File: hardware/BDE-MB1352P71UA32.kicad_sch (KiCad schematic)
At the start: 11 parts, among them J22 Conn_ARM_JTAG_SWD_10, SW1 SW_Push, U1 USBLC6-2P6, U23 BDE-MB1352P71UA32, U3 USBLC6-2P6

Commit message: updated annotations
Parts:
- renumbered C1 to C401, C10 to C402, C2 to C403, D7 to D401, J22 to J401, R7 to R401, R3 to R402, SW1 to SW401, U1 to U401, U3 to U402, U23 to U403
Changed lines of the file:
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@@
 		(dnp no)
 		(fields_autoplaced yes)
-		(property "Reference" "#PWR075"
+		(property "Reference" "#PWR0409"
 			(at 142.24 143.51 0)
 			(effects
@@
 			(project "Senior_Design"
 				(path "/8f5928e8-0fc1-4443-a20f-3bfeb956761e/dd2813e4-a810-44d7-8b7e-d46ce1c3fa30"
-					(reference "#PWR075")
+					(reference "#PWR0409")
 					(unit 1)
 				)
@@
 		(dnp no)
 		(fields_autoplaced yes)
-		(property "Reference" "#PWR072"
+		(property "Reference" "#PWR0411"
 			(at 152.4 78.74 0)
 			(effects
@@
 			(project "Senior_Design"
 				(path "/8f5928e8-0fc1-4443-a20f-3bfeb956761e/dd2813e4-a810-44d7-8b7e-d46ce1c3fa30"
-					(reference "#PWR072")
+					(reference "#PWR0411")
 					(unit 1)
 				)
@@
 		(on_board yes)
 		(dnp no)
-		(property "Reference" "U3"
+		(property "Reference" "U402"
 			(at 136.906 138.684 0)
 			(effects
@@
 			(project "Senior_Design"
 				(path "/8f5928e8-0fc1-4443-a20f-3bfeb956761e/dd2813e4-a810-44d7-8b7e-d46ce1c3fa30"
-					(reference "U3")
+					(reference "U402")
 					(unit 1)
 				)
@@
 		(dnp no)
 		(fields_autoplaced yes)
-		(property "Reference" "#PWR021"
+		(property "Reference" "#PWR0406"
 			(at 129.54 76.2 0)
 			(effects
@@
 			(project "Senior_Design"
 				(path "/8f5928e8-0fc1-4443-a20f-3bfeb956761e/dd2813e4-a810-44d7-8b7e-d46ce1c3fa30"
-					(reference "#PWR021")
+					(reference "#PWR0406")
 					(unit 1)
 				)
@@
 		(on_board yes)
 		(dnp no)
-		(property "Reference" "C10"
+		(property "Reference" "C402"
 			(at 223.52 49.5299 0)
 			(effects
@@
 			(project "Senior_Design"
 				(path "/8f5928e8-0fc1-4443-a20f-3bfeb956761e/dd2813e4-a810-44d7-8b7e-d46ce1c3fa30"
-					(reference "C10")
+					(reference "C402")
 					(unit 1)
 				)
@@
 		(dnp no)
 		(fields_autoplaced yes)
-		(property "Reference" "J22"
+		(property "Reference" "J401"
 			(at 64.77 99.0599 0)
 			(effects
@@
 			(project "Senior_Design"
 				(path "/8f5928e8-0fc1-4443-a20f-3bfeb956761e/dd2813e4-a810-44d7-8b7e-d46ce1c3fa30"
-					(reference "J22")
+					(reference "J401")
 					(unit 1)
 				)
@@
 		(on_board yes)
 		(dnp no)
-		(property "Reference" "U1"
+		(property "Reference" "U401"
 			(at 99.822 138.938 0)
 			(effects
@@
 			(project "Senior_Design"
 				(path "/8f5928e8-0fc1-4443-a20f-3bfeb956761e/dd2813e4-a810-44d7-8b7e-d46ce1c3fa30"
-					(reference "U1")
+					(reference "U401")
 					(unit 1)
 				)
@@
 		(dnp no)
 		(fields_autoplaced yes)
-		(property "Reference" "#PWR0107"
+		(property "Reference" "#PWR0402"
 			(at 76.2 124.46 0)
 			(effects
@@
 			(project "Senior_Design"
 				(path "/8f5928e8-0fc1-4443-a20f-3bfeb956761e/dd2813e4-a810-44d7-8b7e-d46ce1c3fa30"
-					(reference "#PWR0107")
+					(reference "#PWR0402")
 					(unit 1)
 				)
@@
 		(on_board yes)
 		(dnp no)
-		(property "Reference" "C1"
+		(property "Reference" "C401"
 			(at 136.906 67.31 0)
 			(effects
@@
 			(project "Senior_Design"
 				(path "/8f5928e8-0fc1-4443-a20f-3bfeb956761e/dd2813e4-a810-44d7-8b7e-d46ce1c3fa30"
-					(reference "C1")
+					(reference "C401")
 					(unit 1)
 				)
@@
 		(dnp no)
 		(fields_autoplaced yes)
-		(property "Reference" "#PWR018"
+		(property "Reference" "#PWR0408"
 			(at 140.97 76.2 0)
 			(effects
@@
 			(project "Senior_Design"
 				(path "/8f5928e8-0fc1-4443-a20f-3bfeb956761e/dd2813e4-a810-44d7-8b7e-d46ce1c3fa30"
-					(reference "#PWR018")
+					(reference "#PWR0408")
 					(unit 1)
 				)
@@
 		(dnp no)
 		(fields_autoplaced yes)
-		(property "Reference" "#PWR074"
+		(property "Reference" "#PWR0403"
 			(at 105.41 143.51 0)
 			(effects
@@
 			(project "Senior_Design"
 				(path "/8f5928e8-0fc1-4443-a20f-3bfeb956761e/dd2813e4-a810-44d7-8b7e-d46ce1c3fa30"
-					(reference "#PWR074")
+					(reference "#PWR0403")
 					(unit 1)
 				)
@@
 		(dnp no)
 		(fields_autoplaced yes)
-		(property "Reference" "U23"
+		(property "Reference" "U403"
 			(at 189.23 49.53 0)
 			(effects
@@
 			(project "Senior_Design"
 				(path "/8f5928e8-0fc1-4443-a20f-3bfeb956761e/dd2813e4-a810-44d7-8b7e-d46ce1c3fa30"
-					(reference "U23")
+					(reference "U403")
 					(unit 1)
 				)
@@
 		(dnp no)
 		(fields_autoplaced yes)
-		(property "Reference" "#PWR071"
+		(property "Reference" "#PWR0407"
 			(at 140.97 53.34 0)
 			(effects
@@
 			(project "Senior_Design"
 				(path "/8f5928e8-0fc1-4443-a20f-3bfeb956761e/dd2813e4-a810-44d7-8b7e-d46ce1c3fa30"
-					(reference "#PWR071")
+					(reference "#PWR0407")
 					(unit 1)
 				)
@@
 		(dnp no)
 		(fields_autoplaced yes)
-		(property "Reference" "SW1"
+		(property "Reference" "SW401"
 			(at 120.65 54.61 0)
 			(effects
@@
 			(project "Senior_Design"
 				(path "/8f5928e8-0fc1-4443-a20f-3bfeb956761e/dd2813e4-a810-44d7-8b7e-d46ce1c3fa30"
-					(reference "SW1")
+					(reference "SW401")
 					(unit 1)
 				)
@@
 		(dnp no)
 		(fields_autoplaced yes)
-		(property "Reference" "#PWR073"
+		(property "Reference" "#PWR0401"
 			(at 76.2 83.82 0)
 			(effects
@@
 			(project "Senior_Design"
 				(path "/8f5928e8-0fc1-4443-a20f-3bfeb956761e/dd2813e4-a810-44d7-8b7e-d46ce1c3fa30"
-					(reference "#PWR073")
+					(reference "#PWR0401")
 					(unit 1)
 				)
@@
 		(on_board yes)
 		(dnp no)
-		(property "Reference" "D7"
+		(property "Reference" "D401"
 			(at 127 66.9926 90)
 			(effects
@@
 			(project "Senior_Design"
 				(path "/8f5928e8-0fc1-4443-a20f-3bfeb956761e/dd2813e4-a810-44d7-8b7e-d46ce1c3fa30"
-					(reference "D7")
+					(reference "D401")
 					(unit 1)
 				)
@@
 		(dnp no)
 		(fields_autoplaced yes)
-		(property "Reference" "#PWR0106"
+		(property "Reference" "#PWR0412"
 			(at 213.36 120.65 0)
 			(effects
@@
 			(project "Senior_Design"
 				(path "/8f5928e8-0fc1-4443-a20f-3bfeb956761e/dd2813e4-a810-44d7-8b7e-d46ce1c3fa30"
-					(reference "#PWR0106")
+					(reference "#PWR0412")
 					(unit 1)
 				)
@@
 		(dnp no)
 		(fields_autoplaced yes)
-		(property "Reference" "#PWR09"
+		(property "Reference" "#PWR0405"
 			(at 115.57 69.85 0)
 			(effects
@@
 			(project "Senior_Design"
 				(path "/8f5928e8-0fc1-4443-a20f-3bfeb956761e/dd2813e4-a810-44d7-8b7e-d46ce1c3fa30"
-					(reference "#PWR09")
+					(reference "#PWR0405")
 					(unit 1)
 				)
@@
 		(dnp no)
 		(fields_autoplaced yes)
-		(property "Reference" "C2"
+		(property "Reference" "C403"
 			(at 236.22 50.7999 0)
 			(effects
@@
 			(project "Senior_Design"
 				(path "/8f5928e8-0fc1-4443-a20f-3bfeb956761e/dd2813e4-a810-44d7-8b7e-d46ce1c3fa30"
-					(reference "C2")
+					(reference "C403")
 					(unit 1)
 				)
@@
 		(dnp no)
 		(fields_autoplaced yes)
-		(property "Reference" "#PWR01"
+		(property "Reference" "#PWR0404"
 			(at 105.41 158.75 0)
 			(effects
@@
 			(project "Senior_Design"
 				(path "/8f5928e8-0fc1-4443-a20f-3bfeb956761e/dd2813e4-a810-44d7-8b7e-d46ce1c3fa30"
-					(reference "#PWR01")
+					(reference "#PWR0404")
 					(unit 1)
 				)
@@
 		(on_board yes)
 		(dnp no)
-		(property "Reference" "R7"
+		(property "Reference" "R401"
 			(at 143.51 54.6099 0)
 			(effects
@@
 			(project "Senior_Design"
 				(path "/8f5928e8-0fc1-4443-a20f-3bfeb956761e/dd2813e4-a810-44d7-8b7e-d46ce1c3fa30"
-					(reference "R7")
+					(reference "R401")
 					(unit 1)
 				)
@@
 		(dnp no)
 		(fields_autoplaced yes)
-		(property "Reference" "#PWR02"
+		(property "Reference" "#PWR0410"
 			(at 142.24 158.75 0)
 			(effects
@@
 			(project "Senior_Design"
 				(path "/8f5928e8-0fc1-4443-a20f-3bfeb956761e/dd2813e4-a810-44d7-8b7e-d46ce1c3fa30"
-					(reference "#PWR02")
+					(reference "#PWR0410")
 					(unit 1)
 				)
@@
 		(on_board yes)
 		(dnp no)
-		(property "Reference" "R3"
+		(property "Reference" "R402"
 			(at 147.32 77.47 0)
 			(effects
@@
 			(project "Senior_Design"
 				(path "/8f5928e8-0fc1-4443-a20f-3bfeb956761e/dd2813e4-a810-44d7-8b7e-d46ce1c3fa30"
-					(reference "R3")
+					(reference "R402")
 					(unit 1)
 				)
@@
 		(on_board yes)
 		(dnp no)
-		(property "Reference" "#FLG0106"
+		(property "Reference" "#FLG0401"
 			(at 213.36 48.895 0)
 			(effects
@@
 			(project "Senior_Design"
 				(path "/8f5928e8-0fc1-4443-a20f-3bfeb956761e/dd2813e4-a810-44d7-8b7e-d46ce1c3fa30"
-					(reference "#FLG0106")
+					(reference "#FLG0401")
 					(unit 1)
 				)
@@
 		(dnp no)
 		(fields_autoplaced yes)
-		(property "Reference" "#PWR076"
+		(property "Reference" "#PWR0413"
 			(at 232.41 49.53 0)
 			(effects
@@
 			(project "Senior_Design"
 				(path "/8f5928e8-0fc1-4443-a20f-3bfeb956761e/dd2813e4-a810-44d7-8b7e-d46ce1c3fa30"
-					(reference "#PWR076")
-					(unit 1)
-				)
+					(reference "#PWR0413")
+					(unit 1)
+				)

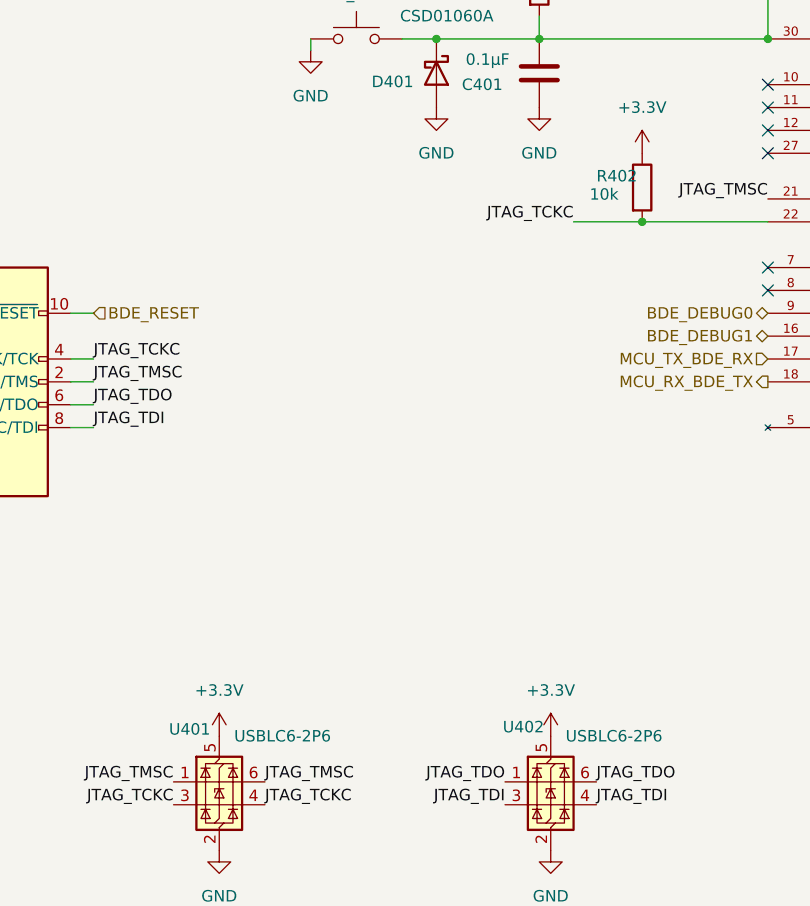
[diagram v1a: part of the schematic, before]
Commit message: added ship fet
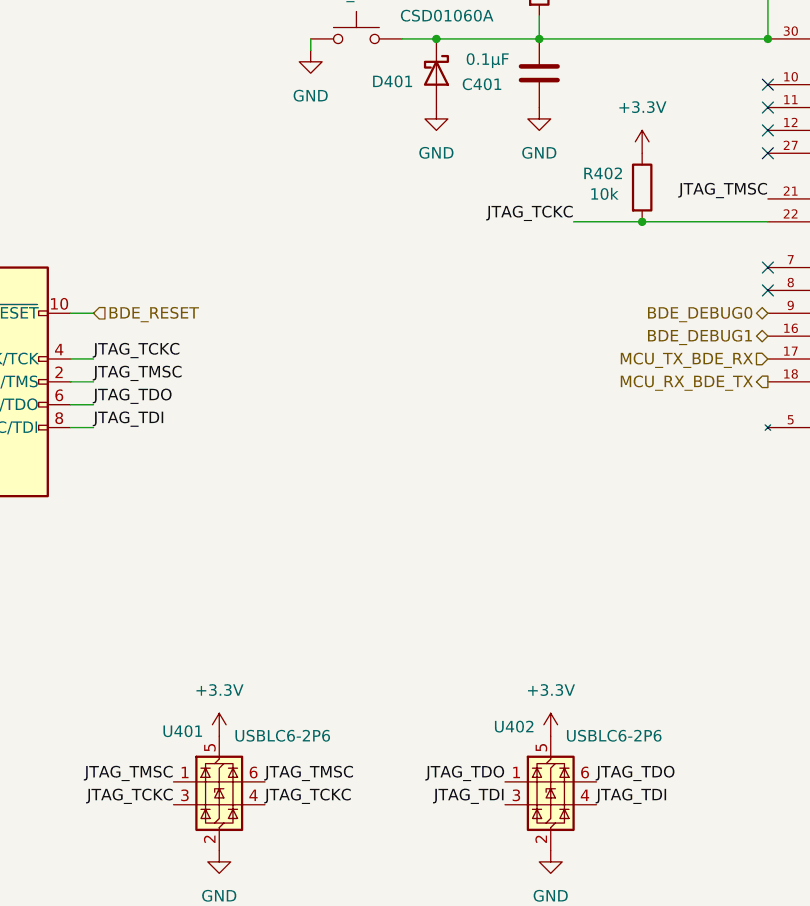
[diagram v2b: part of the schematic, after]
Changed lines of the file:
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@@
 		(dnp no)
 		(property "Reference" "U402"
-			(at 136.906 138.684 0)
+			(at 135.89 138.684 0)
 			(effects
 				(font
@@
 		(dnp no)
 		(property "Reference" "U401"
-			(at 99.822 138.938 0)
+			(at 99.06 139.192 0)
 			(effects
 				(font
@@
 		(dnp no)
 		(property "Reference" "R402"
-			(at 147.32 77.47 0)
-			(effects
-				(font
+			(at 145.796 77.216 0)
+			(effects
+				(font

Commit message: footprint update
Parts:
- C401: footprint Capacitor_SMD:C_0603_1608Metric -> Capacitor_SMD:C_0805_2012Metric
- C402, C403: footprint Capacitor_SMD:C_0402_1005Metric -> Capacitor_SMD:C_0805_2012Metric
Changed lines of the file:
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@@
 			)
 		)
-		(property "Footprint" "Capacitor_SMD:C_0402_1005Metric"
+		(property "Footprint" "Capacitor_SMD:C_0805_2012Metric"
 			(at 220.6752 55.88 0)
 			(effects
@@
 			)
 		)
-		(property "Footprint" "Capacitor_SMD:C_0603_1608Metric"
+		(property "Footprint" "Capacitor_SMD:C_0805_2012Metric"
 			(at 141.9352 69.85 0)
 			(effects
@@
 			)
 		)
-		(property "Footprint" "Capacitor_SMD:C_0402_1005Metric"
+		(property "Footprint" "Capacitor_SMD:C_0805_2012Metric"
 			(at 233.3752 55.88 0)
 			(effects

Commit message: footprint update 2
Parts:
- D401: footprint Package_TO_SOT_THT:TO-220-2_Vertical -> Diode_SMD:D_SOD-123
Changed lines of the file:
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@@
 			)
 		)
-		(property "Footprint" "Package_TO_SOT_THT:TO-220-2_Vertical"
+		(property "Footprint" "Diode_SMD:D_SOD-123"
 			(at 125.095 66.04 0)
 			(effects

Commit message: updated footprints
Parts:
- J401: footprint Connector_PinHeader_1.27mm:PinHeader_2x05_P1.27mm_Vertical -> Connector_PinHeader_1.27mm:PinHeader_2x05_P1.27mm_Vertical_SMD
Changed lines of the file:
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@@
 			)
 		)
-		(property "Footprint" "Connector_PinHeader_1.27mm:PinHeader_2x05_P1.27mm_Vertical"
+		(property "Footprint" "Connector_PinHeader_1.27mm:PinHeader_2x05_P1.27mm_Vertical_SMD"
 			(at 76.2 100.33 0)
 			(effects
